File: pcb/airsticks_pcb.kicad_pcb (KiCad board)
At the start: 2 copper layers, 66.5 x 22.5 mm, 17 parts, among them J1 USB_C_Receptacle_USB2.0, J2 STM_LINK, J3 USB_SERIAL_TTL, J4 I2C, J5 AudioJack3, U1 STM32G441KBT6, U4 PAM8302AAS, U5 TC1262-33

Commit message: finished pcb
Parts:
- removed the J4 at (49.9, 73.8)
- added ?: , , F.Cu at (59.6, 67.2)
- added ?: , , F.Cu at (59.6, 56.0)
- added ?: , , F.Cu at (64.9, 65.0)
- added ?: , , F.Cu at (59.6, 59.7)
- added ?: , , F.Cu at (59.6, 65.8)
- added ?: , , F.Cu at (64.2, 65.0)
- added ?: , , F.Cu at (59.6, 56.7)
- added ?: , , F.Cu at (59.6, 57.5)
- added ?: , , F.Cu at (59.6, 75.5)
- added ?: , , F.Cu at (59.6, 62.8)
- added ?: , , F.Cu at (59.6, 68.8)
- added ?: , , F.Cu at (57.3, 72.4)
- added ?: , , F.Cu at (59.6, 64.2)
- added ?: , , F.Cu at (61.9, 74.5)
- added ?: , , F.Cu at (59.6, 71.0)
- added ? (x2): , , F.Cu at (65.7, 65.0)
- added ?: , , F.Cu at (59.6, 73.3)
- added ?: , , F.Cu at (59.6, 69.5)
- added ?: , , F.Cu at (59.6, 63.5)
- added ?: , , F.Cu at (59.6, 59.0)
- added ?: , , F.Cu at (59.6, 65.0)
- added ?: , , F.Cu at (67.2, 65.0)
- added ?: , , F.Cu at (62.6, 65.0)
- added ?: , , F.Cu at (63.4, 65.0)
- added ?: , , F.Cu at (64.7, 55.8)
- added ?: , , F.Cu at (59.6, 74.8)
- added ?: , , F.Cu at (59.6, 55.2)
- added ?: , , F.Cu at (59.6, 72.5)
- added ?: , , F.Cu at (53.3, 73.8)
- added ?: , , F.Cu at (61.1, 65.0)
- added ?: , , F.Cu at (59.6, 62.0)
- added ?: , , F.Cu at (59.6, 61.2)
- added ?: , , F.Cu at (59.6, 68.0)
- added ?: , , F.Cu at (59.6, 70.3)
- added ?: , , F.Cu at (59.6, 66.5)
- added ?: , , F.Cu at (61.7, 63.3)
- added ?: , , F.Cu at (64.7, 66.9)
- added ?: , , F.Cu at (60.4, 65.0)
- added ?: , , F.Cu at (50.6, 73.8)
- added ?: , , F.Cu at (59.6, 58.2)
- added ?: , , F.Cu at (67.9, 65.0)
- added ?: , , F.Cu at (59.6, 60.5)
- added ?: , , F.Cu at (59.6, 74.0)
- added ?: , , F.Cu at (59.6, 71.8)
- added ?: , , F.Cu at (59.6, 54.5)
- added ?: , , F.Cu at (66.4, 65.0)
- added ?: , , F.Cu at (61.9, 65.0)
- added J4: I2C, Connector_PinHeader_2.54mm:PinHeader_1x03_P2.54mm_Vertical, F.Cu at (57.3, 69.8)
- added J4: I2C, Connector_PinHeader_2.54mm:PinHeader_1x03_P2.54mm_Vertical, F.Cu at (61.9, 72.0)
- added J4: I2C, Connector_PinHeader_2.54mm:PinHeader_1x03_P2.54mm_Vertical, F.Cu at (61.7, 60.8)
- added REF**: SolderJumper-2_P1.3mm_Open_TrianglePad1.0x1.5mm, Jumper:SolderJumper-2_P1.3mm_Open_TrianglePad1.0x1.5mm, F.Cu at (47.1, 73.8)
- added REF**: SolderJumper-2_P1.3mm_Open_TrianglePad1.0x1.5mm, Jumper:SolderJumper-2_P1.3mm_Open_TrianglePad1.0x1.5mm, B.Cu at (48.3, 70.7)
- C5, C6: moved to B.Cu
- moved xlr_left1 21.4 mm to (65.7, 70.8), turned to 90 degrees
- moved C5 16.6 mm to (34.6, 61.8), turned to 0 degrees
- moved C6 11.5 mm to (40.8, 63.4), turned to 90 degrees
- moved xlr_right1 7.72 mm to (65.7, 59.5), turned to 90 degrees
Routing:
- net +3V3: track 10.3 -> 48.9 mm, vias 4 -> 7
- net GND: track 20.3 -> 58.0 mm, vias 2 -> 5
- net /I2C1_SDA: track 0.00 -> 26.9 mm, vias 0 -> 2
- net +5V: track 80.6 -> 57.1 mm, vias 4 -> 3
- net /ACC_INT1: track 0.00 -> 21.5 mm, vias 0 -> 1
- net /I2C1_SLC: track 0.00 -> 21.1 mm
- net /ACC_INT0: track 0.00 -> 12.9 mm
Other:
- board size 66.5 x 22.5 mm -> 48.7 x 22.5 mm

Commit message: small changes to final pcb layout
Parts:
- removed the ? at (64.7, 55.8)
- removed the ? at (61.7, 63.3)
- added ?: , , F.Cu at (61.7, 63.3)
- added ?: , , F.Cu at (64.2, 55.7)
- moved ? 0.35 mm to (64.4, 66.9)
- moved ? 0.17 mm to (53.1, 73.8)

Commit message: pcb ready for printing
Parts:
- removed C2: 0.1uF, Capacitor_SMD:C_0805_2012Metric_Pad1.18x1.45mm_HandSolder
- removed the REF** at (47.1, 73.8)
- added REF**: SolderJumper-2_P1.3mm_Open_TrianglePad1.0x1.5mm, Jumper:SolderJumper-2_P1.3mm_Open_TrianglePad1.0x1.5mm, F.Cu at (47.1, 74.0)
- added REF**: SolderJumper-2_P1.3mm_Open_TrianglePad1.0x1.5mm, Jumper:SolderJumper-2_P1.3mm_Open_TrianglePad1.0x1.5mm, B.Cu at (48.0, 71.8)
- moved C6 3.72 mm to (40.0, 59.8), turned to 180 degrees
- moved REF** 1.43 mm to (48.0, 69.3)
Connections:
- U1 pad 9: unconnected-(U1-Pad9) -> /AUDIO+
- U4 pad 4: Net-(C2-Pad2) -> Net-(C1-Pad2)
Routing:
- net /AUDIO+: track 0.00 -> 31.5 mm, vias 0 -> 2
- net GND: track 57.7 -> 68.3 mm
- net Net-(C2-Pad2): track 2.65 -> 0.00 mm
- net /ACC_INT0: track 13.1 -> 14.8 mm, vias 0 -> 1
- net Net-(R1-Pad2): track 14.7 -> 16.3 mm
- net Net-(C1-Pad2): track 5.19 -> 6.34 mm
- net /ACC_INT1: track 21.6 -> 20.6 mm

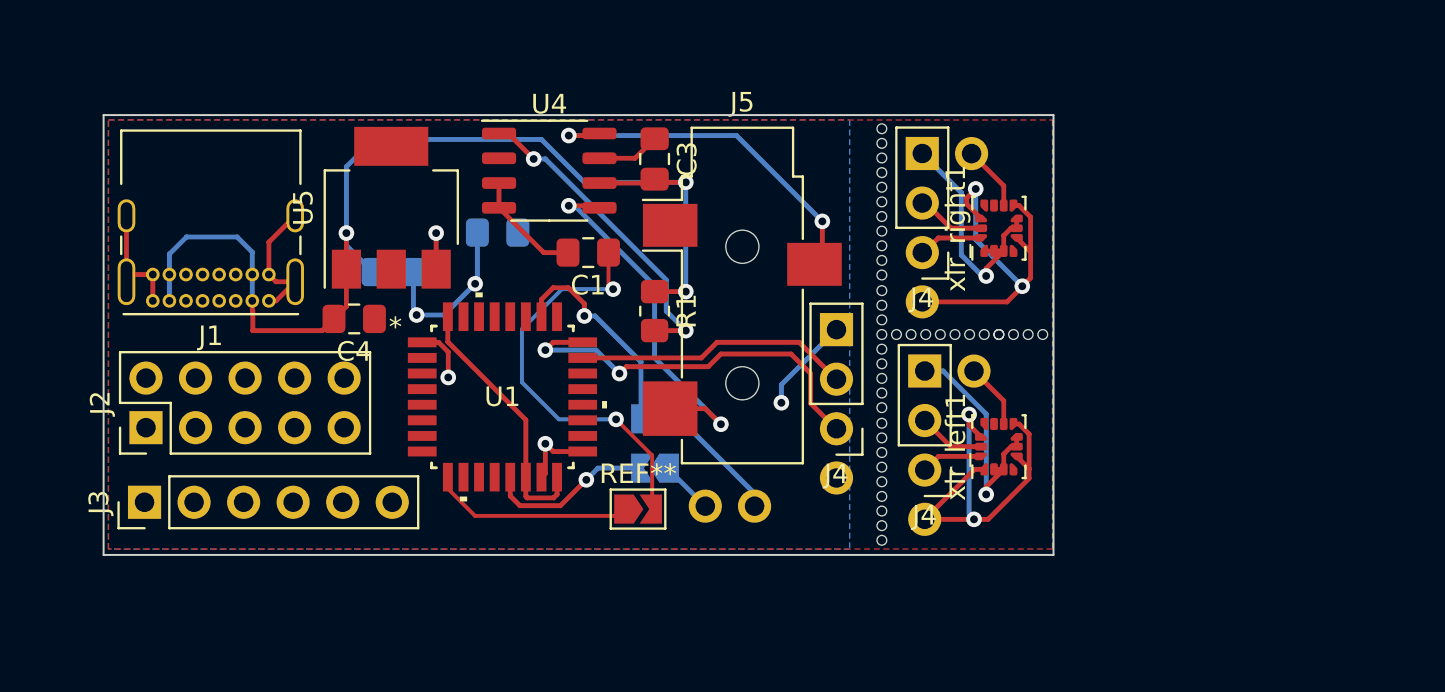
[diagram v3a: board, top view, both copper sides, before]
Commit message: updated accelerometer sensitivity to 8G
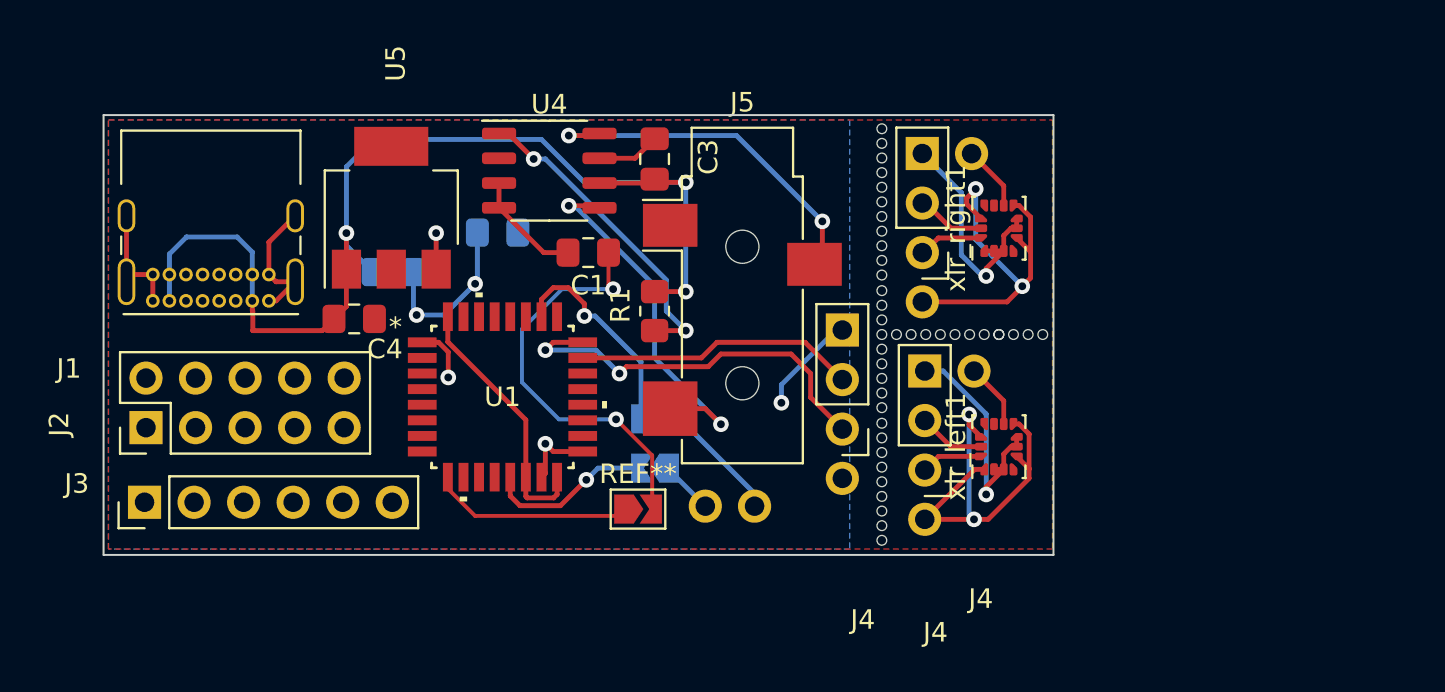
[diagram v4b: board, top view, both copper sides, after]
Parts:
- moved ? 0.30 mm to (57.6, 72.4)
- moved J4 0.30 mm to (57.6, 69.8)
